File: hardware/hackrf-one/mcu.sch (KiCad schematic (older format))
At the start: 112 parts, among them J1 GSG-USB-MICRO-B, P1 1V8, P13 VBUS, P17 SSP0, P20 GPIO, P21 ANALOG, P22 I2S, P23 DBGEN, P24 TRST, P25 LPC_ISP, P26 LPC_JTAG, P28 SD, P29 CPLD_JTAG, P3 GND, P30 BANK2_AUX, P31 BANK1_AUX, P5 WAKEUP, P7 RTC, P8 VCC, SW1 DFU, SW2 RESET, U20 W25Q80BV, U21 TPS62410, U22 GSG-IP4220CZ6, U23 LPC4320FBD144, U24 GSG-XC2C64A-7VQG100C, X2 MCU_XTAL, X3 RTC_XTAL

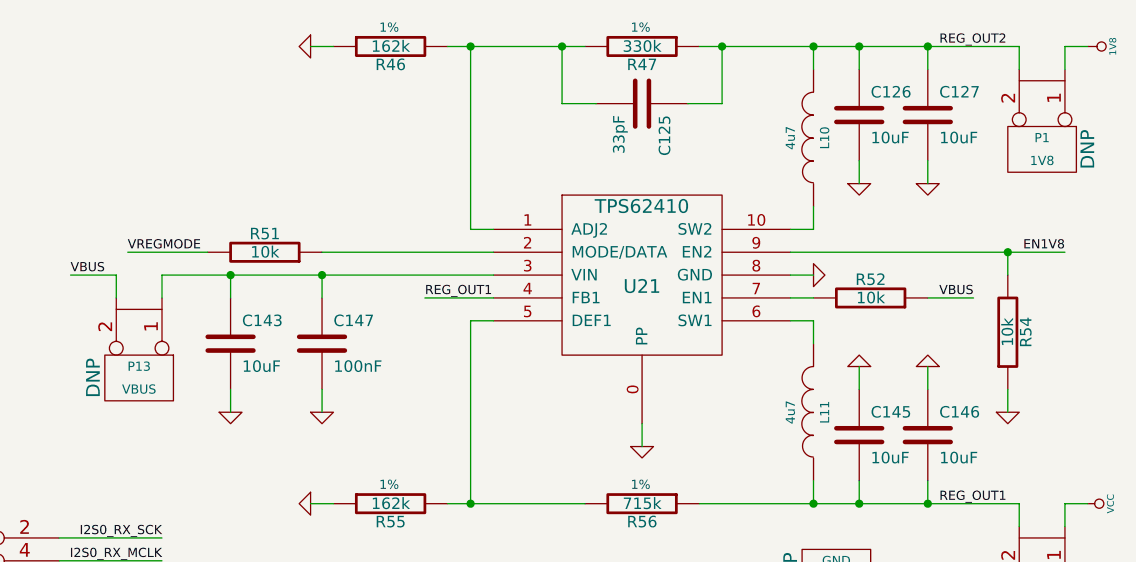
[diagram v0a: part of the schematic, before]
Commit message: USB, regulator layout
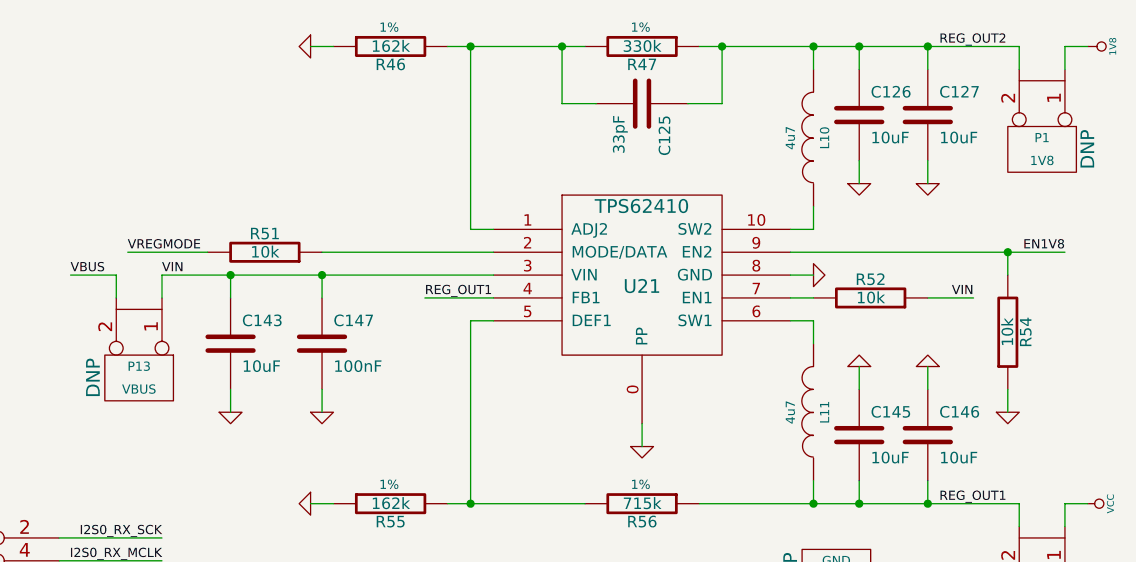
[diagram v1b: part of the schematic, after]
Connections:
- net labels added: VIN
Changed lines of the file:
@@
 EN1V8
 Text Label 15750 1750 2    40   ~ 0
-VBUS
+VIN
 $Comp
 L GND #PWR0199
@@
 NoConn ~ 11600 7850
 NoConn ~ 15600 6450
+Text Label 12200 1650 0    40   ~ 0
+VIN
 $EndSCHEMATC

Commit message: SPI flash layout
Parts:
- X3: Description (none) -> CRYSTAL 32.768KHZ 12.5PF THRU; Manufacturer (none) -> Abracon; Part Number (none) -> AB26T-32.768KHZ
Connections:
- wire segments 517 -> 520
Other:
- moved on the sheet: C136, C137, C138, C139, C140, C141, C142
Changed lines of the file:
@@
 Sheet 4 4
 Title "HackRF One mcu/usb/power"
-Date "1 nov 2013"
+Date "6 nov 2013"
 Rev ""
 Comp "Copyright 2012 Michael Ossmann"
@@
 L C C142
 U 1 1 503C4C2C
-P 5050 1000
-F 0 "C142" H 5100 1100 50  0000 L CNN
-F 1 "100nF" H 5100 900 50  0000 L CNN
-F 2 "" H 5050 1000 60  0001 C CNN
-F 3 "" H 5050 1000 60  0001 C CNN
-F 4 "Murata" H 5050 1000 60  0001 C CNN "Manufacturer"
-F 5 "GRM155R61A104KA01D" H 5050 1000 60  0001 C CNN "Part Number"
-F 6 "CAP CER 0.1UF 10V 10% X5R 0402" H 5050 1000 60  0001 C CNN "Description"
-	1    5050 1000
-	1    0    0    -1
-$EndComp
-$Comp
-L C C141
-U 1 1 503C4C2A
 P 4750 1000
-F 0 "C141" H 4800 1100 50  0000 L CNN
+F 0 "C142" H 4800 1100 50  0000 L CNN
 F 1 "100nF" H 4800 900 50  0000 L CNN
 F 2 "" H 4750 1000 60  0001 C CNN
@@
 $EndComp
 $Comp
-L C C140
-U 1 1 503C4C29
+L C C141
+U 1 1 503C4C2A
 P 4450 1000
-F 0 "C140" H 4500 1100 50  0000 L CNN
+F 0 "C141" H 4500 1100 50  0000 L CNN
 F 1 "100nF" H 4500 900 50  0000 L CNN
 F 2 "" H 4450 1000 60  0001 C CNN
@@
 $EndComp
 $Comp
-L C C139
-U 1 1 503C4C28
+L C C140
+U 1 1 503C4C29
 P 4150 1000
-F 0 "C139" H 4200 1100 50  0000 L CNN
+F 0 "C140" H 4200 1100 50  0000 L CNN
 F 1 "100nF" H 4200 900 50  0000 L CNN
 F 2 "" H 4150 1000 60  0001 C CNN
@@
 $EndComp
 $Comp
-L C C138
-U 1 1 503C4C27
+L C C139
+U 1 1 503C4C28
 P 3850 1000
-F 0 "C138" H 3900 1100 50  0000 L CNN
+F 0 "C139" H 3900 1100 50  0000 L CNN
 F 1 "100nF" H 3900 900 50  0000 L CNN
 F 2 "" H 3850 1000 60  0001 C CNN
@@
 $EndComp
 $Comp
-L C C137
-U 1 1 503C4C25
+L C C138
+U 1 1 503C4C27
 P 3550 1000
-F 0 "C137" H 3600 1100 50  0000 L CNN
+F 0 "C138" H 3600 1100 50  0000 L CNN
 F 1 "100nF" H 3600 900 50  0000 L CNN
 F 2 "" H 3550 1000 60  0001 C CNN
@@
 $EndComp
 $Comp
-L C C136
-U 1 1 503C4C24
+L C C137
+U 1 1 503C4C25
 P 3250 1000
-F 0 "C136" H 3300 1100 50  0000 L CNN
+F 0 "C137" H 3300 1100 50  0000 L CNN
 F 1 "100nF" H 3300 900 50  0000 L CNN
 F 2 "" H 3250 1000 60  0001 C CNN
@@
 $EndComp
 $Comp
+L C C136
+U 1 1 503C4C24
+P 5400 1200
+F 0 "C136" H 5450 1300 50  0000 L CNN
+F 1 "100nF" H 5450 1100 50  0000 L CNN
+F 2 "" H 5400 1200 60  0001 C CNN
+F 3 "" H 5400 1200 60  0001 C CNN
+F 4 "Murata" H 5400 1200 60  0001 C CNN "Manufacturer"
+F 5 "GRM155R61A104KA01D" H 5400 1200 60  0001 C CNN "Part Number"
+F 6 "CAP CER 0.1UF 10V 10% X5R 0402" H 5400 1200 60  0001 C CNN "Description"
+	1    5400 1200
+	0    1    1    0
+$EndComp
+$Comp
 L C C135
 U 1 1 503C4C23
@@
 F 2 "" H 3200 8200 60  0000 C CNN
 F 3 "" H 3200 8200 60  0000 C CNN
-F 4 "DNP" H 3200 7950 60  0000 C CNN "Note"
+F 4 "Abracon" H 3200 8200 60  0001 C CNN "Manufacturer"
+F 5 "AB26T-32.768KHZ" H 3200 8200 60  0001 C CNN "Part Number"
+F 6 "CRYSTAL 32.768KHZ 12.5PF THRU" H 3200 8200 60  0001 C CNN "Description"
+F 7 "DNP" H 3200 7950 60  0000 C CNN "Note"
 	1    3200 8200
 	1    0    0    1
@@
 Wire Wire Line
 	3400 5300 3500 5300
-Connection ~ 4750 1200
-Wire Wire Line
-	700  1200 5050 1200
-Connection ~ 4150 1200
-Connection ~ 3550 1200
-Connection ~ 4450 800
-Connection ~ 3850 800
+Connection ~ 4450 1200
+Connection ~ 3850 1200
 Connection ~ 3250 1200
+Connection ~ 4150 800
+Connection ~ 3550 800
 Connection ~ 2650 1200
 Connection ~ 2050 1200
-Connection ~ 3250 800
 Connection ~ 2650 800
 Connection ~ 2050 800
@@
 Connection ~ 2350 1200
 Connection ~ 2950 1200
-Connection ~ 3550 800
-Connection ~ 4150 800
-Wire Wire Line
-	700  800  5050 800
-Connection ~ 4750 800
-Connection ~ 3850 1200
-Connection ~ 4450 1200
+Connection ~ 3250 800
+Connection ~ 3850 800
+Connection ~ 4450 800
+Connection ~ 3550 1200
+Connection ~ 4150 1200
 Wire Wire Line
 	4000 5300 4300 5300
@@
 Text Label 12200 1650 0    40   ~ 0
 VIN
+Wire Wire Line
+	700  800  4750 800
+Wire Wire Line
+	700  1200 4750 1200
+Wire Wire Line
+	5950 1200 5600 1200
+Connection ~ 5950 1200
+$Comp
+L GND #PWR?
+U 1 1 527ADD81
+P 5100 1300
+F 0 "#PWR?" H 5100 1300 30  0001 C CNN
+F 1 "GND" H 5100 1230 30  0001 C CNN
+F 2 "" H 5100 1300 60  0000 C CNN
+F 3 "" H 5100 1300 60  0000 C CNN
+	1    5100 1300
+	1    0    0    -1
+$EndComp
+Wire Wire Line
+	5100 1300 5100 1200
+Wire Wire Line
+	5100 1200 5200 1200
 $EndSCHEMATC

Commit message: started rearranging expansion headers
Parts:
- removed P31: BANK1_AUX, symbol CONN_5X2
- P28: symbol CONN_6X2 -> CONN_10X2
- P30: symbol CONN_8X2 -> CONN_10X2
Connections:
- wire segments 520 -> 521
- no-connect marks 16 -> 15

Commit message: P20 consolidation
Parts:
- removed P13: VBUS, symbol CONN_2_SHORTED
- removed P21: ANALOG, symbol CONN_4X2
- removed P5: WAKEUP, symbol CONN_1
- removed P7: RTC, symbol CONN_2
- P20: symbol CONN_5X2 -> CONN_12X2
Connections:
- net ADC0_0: now also P20.22 (P22)
- net ADC0_2: now also P20.18 (P18)
- net ADC0_5: now also P20.20 (P20)
- net ADC0_6: now also P20.16 (P16)
- net GND: now also P20.1 (P1), P20.15 (P15), P20.17 (P17), P20.19 (P19), P20.2 (P2), P20.21 (P21); no longer P20.10, P20.9
- net GPIO3_10: now also P20.9 (P9); no longer P20.3
- net GPIO3_11: now also P20.10 (P10); no longer P20.4
- net GPIO3_12: now also P20.11 (P11); no longer P20.5
- net GPIO3_13: now also P20.12 (P12); no longer P20.6
- net GPIO3_14: now also P20.13 (P13); no longer P20.7
- net GPIO3_15: now also P20.14 (P14); no longer P20.8
- net GPIO3_8: now also P20.7 (P7); no longer P20.1
- net GPIO3_9: now also P20.8 (P8); no longer P20.2
- net RTC_ALARM: now also P20.4 (P4)
- net VBAT: now also P20.3 (P3)
- net VBUS: now also P20.24 (P24)
- net VCC: now also P20.5 (P5)
- net VIN: now also P20.23 (P23)
- net WAKEUP: now reaches R48.2, U23.130 (WAKEUP0)
- net WAKEUP: now also P20.6 (P6)
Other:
- note added: "PCB trace jumper"
- moved on the sheet: C118, C136, C164, X3

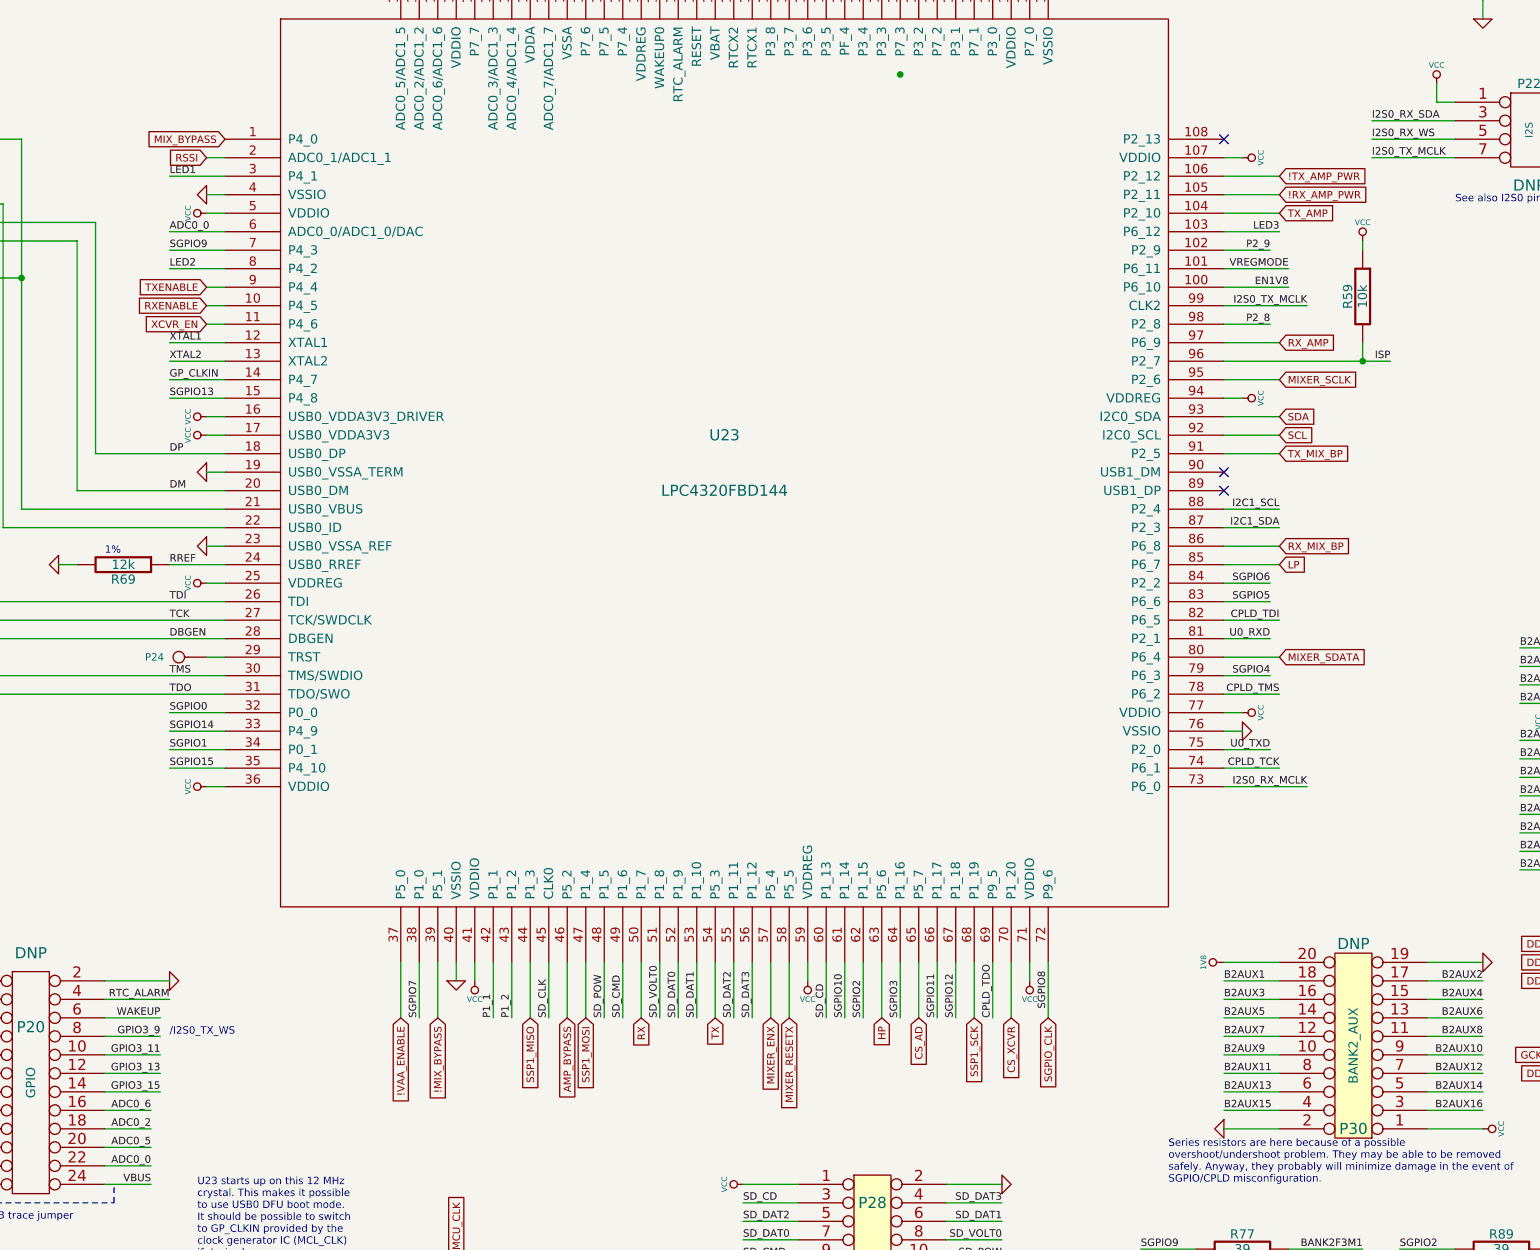
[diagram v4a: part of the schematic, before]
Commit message: finished the trickiest digital signal routing
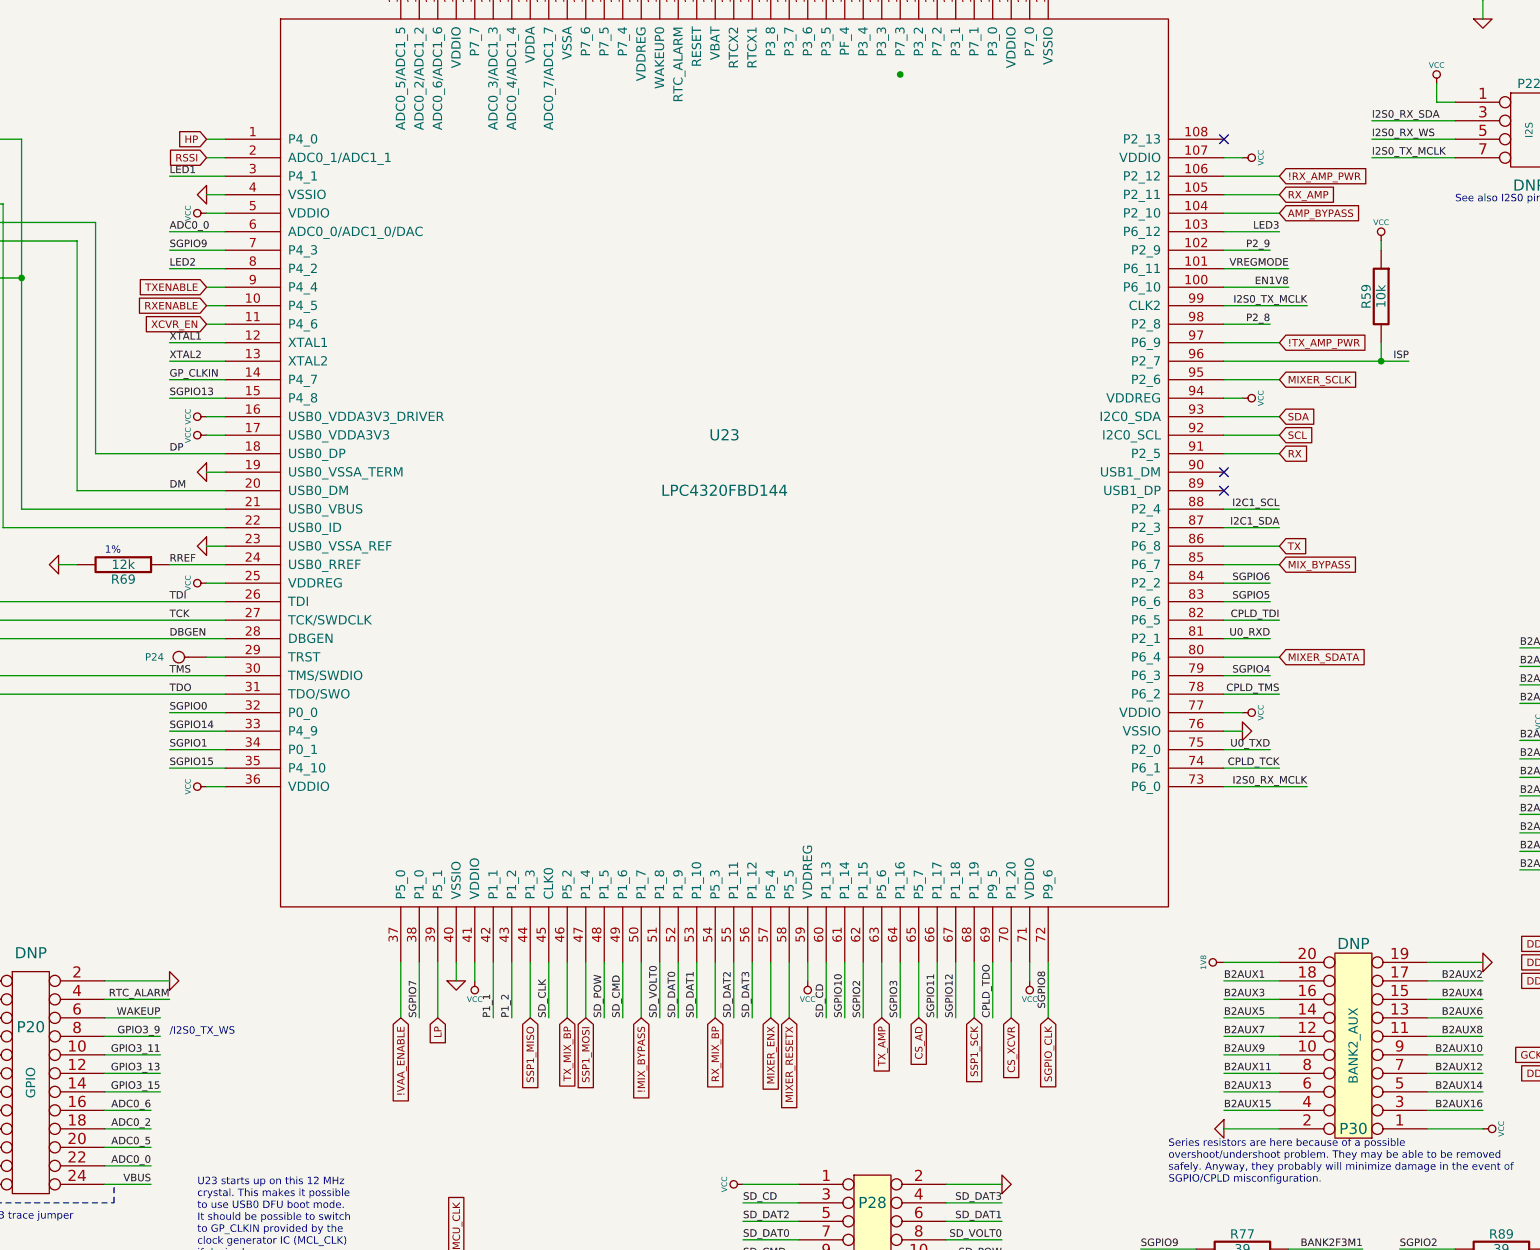
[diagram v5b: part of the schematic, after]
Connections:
- net !MIX_BYPASS: now also U23.50 (P1_7); no longer U23.39 (P5_1)
- net !RX_AMP_PWR: now also U23.106 (P2_12); no longer U23.105 (P2_11)
- net !TX_AMP_PWR: now also U23.97 (P6_9); no longer U23.106 (P2_12)
- net AMP_BYPASS: now also U23.104 (P2_10); no longer U23.46 (P5_2)
- net HP: now also U23.1 (P4_0); no longer U23.63 (P5_6)
- net LP: now also U23.39 (P5_1); no longer U23.85 (P6_7)
- net MIX_BYPASS: now also U23.85 (P6_7); no longer U23.1 (P4_0)
- net RX: now also U23.91 (P2_5); no longer U23.50 (P1_7)
- net RX_AMP: now also U23.105 (P2_11); no longer U23.97 (P6_9)
- net RX_MIX_BP: now also U23.54 (P5_3); no longer U23.86 (P6_8)
- net TX: now also U23.86 (P6_8); no longer U23.54 (P5_3)
- net TX_AMP: now also U23.63 (P5_6); no longer U23.104 (P2_10)
- net TX_MIX_BP: now also U23.46 (P5_2); no longer U23.91 (P2_5)
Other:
- moved on the sheet: R59
